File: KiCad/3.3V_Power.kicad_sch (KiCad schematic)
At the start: 5 parts, among them U2 NCP1117-3.3_SOT223

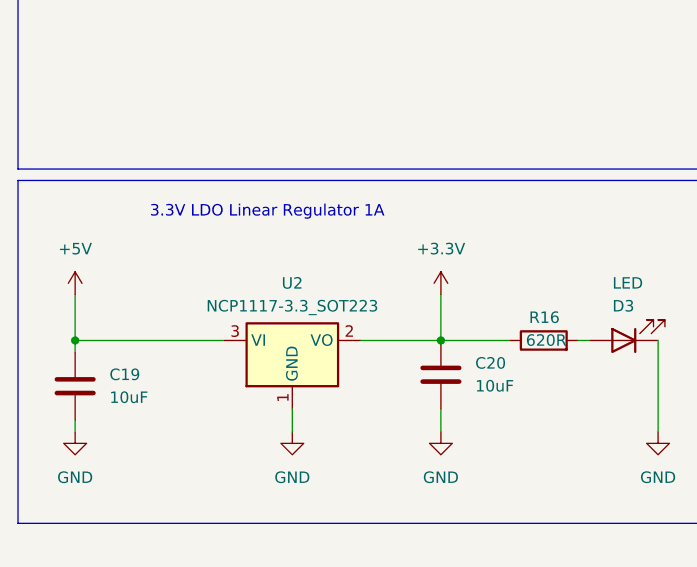
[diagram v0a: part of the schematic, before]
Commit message: Use 12V Power
* Use 12 V Power
* Update to an F103 processor with better compatibility with Katapult
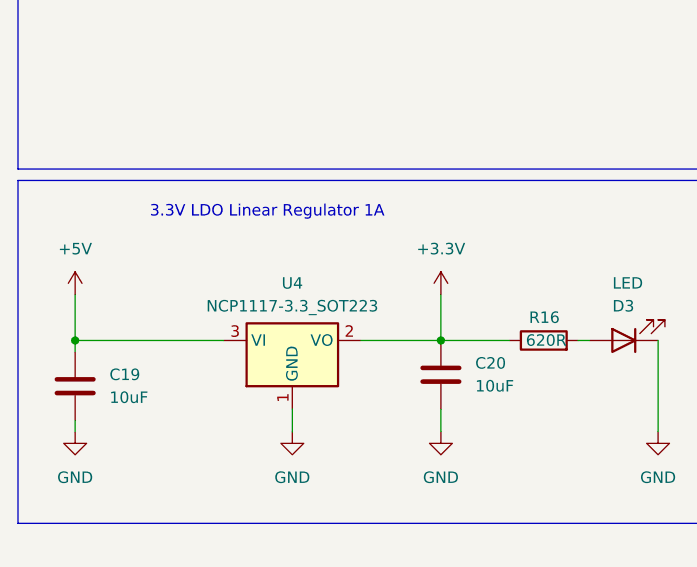
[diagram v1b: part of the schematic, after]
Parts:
- renumbered U2 to U4
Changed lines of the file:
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@@
 		(dnp no)
 		(fields_autoplaced yes)
-		(property "Reference" "U2"
+		(property "Reference" "U4"
 			(at 121.92 81.28 0)
 			(effects
@@
 			(project ""
 				(path "/5d164854-6659-4076-ba4e-df0771b4723d/aa653dec-ec2f-426a-ab21-68104927e222"
-					(reference "U2")
+					(reference "U4")
 					(unit 1)
 				)
